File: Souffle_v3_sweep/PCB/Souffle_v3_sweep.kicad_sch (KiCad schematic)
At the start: 86 parts, among them J1 LED, J2 4PIN, J3 OLED, J4 Conn_01x01_Female, J5 Conn_01x01_Female, J6 Conn_01x01, J7 Conn_01x01, SW1 SW_PUSH, SW10 SW_PUSH, SW11 SW_PUSH, SW12 SW_PUSH, SW13 SW_PUSH, SW14 SW_PUSH, SW15 SW_PUSH, SW16 SW_PUSH, SW17 SW_PUSH, SW18 SW_PUSH, SW19 SW_PUSH, SW2 SW_PUSH, SW20 SW_PUSH, SW21 SW_PUSH, SW22 SW_PUSH, SW23 SW_PUSH, SW24 SW_PUSH, SW25 SW_PUSH, SW25b1 RotaryEncoder_Switch, SW26 SW_PUSH, SW27 SW_PUSH, SW28 SW_PUSH, SW29 SW_PUSH, SW3 SW_PUSH, SW30 SW_PUSH, SW31 SW_SPDT, SW4 SW_PUSH, SW5 SW_PUSH, SW6 SW_PUSH, SW7 SW_PUSH, SW8 SW_PUSH, SW9 SW_PUSH, U1 ProMicro

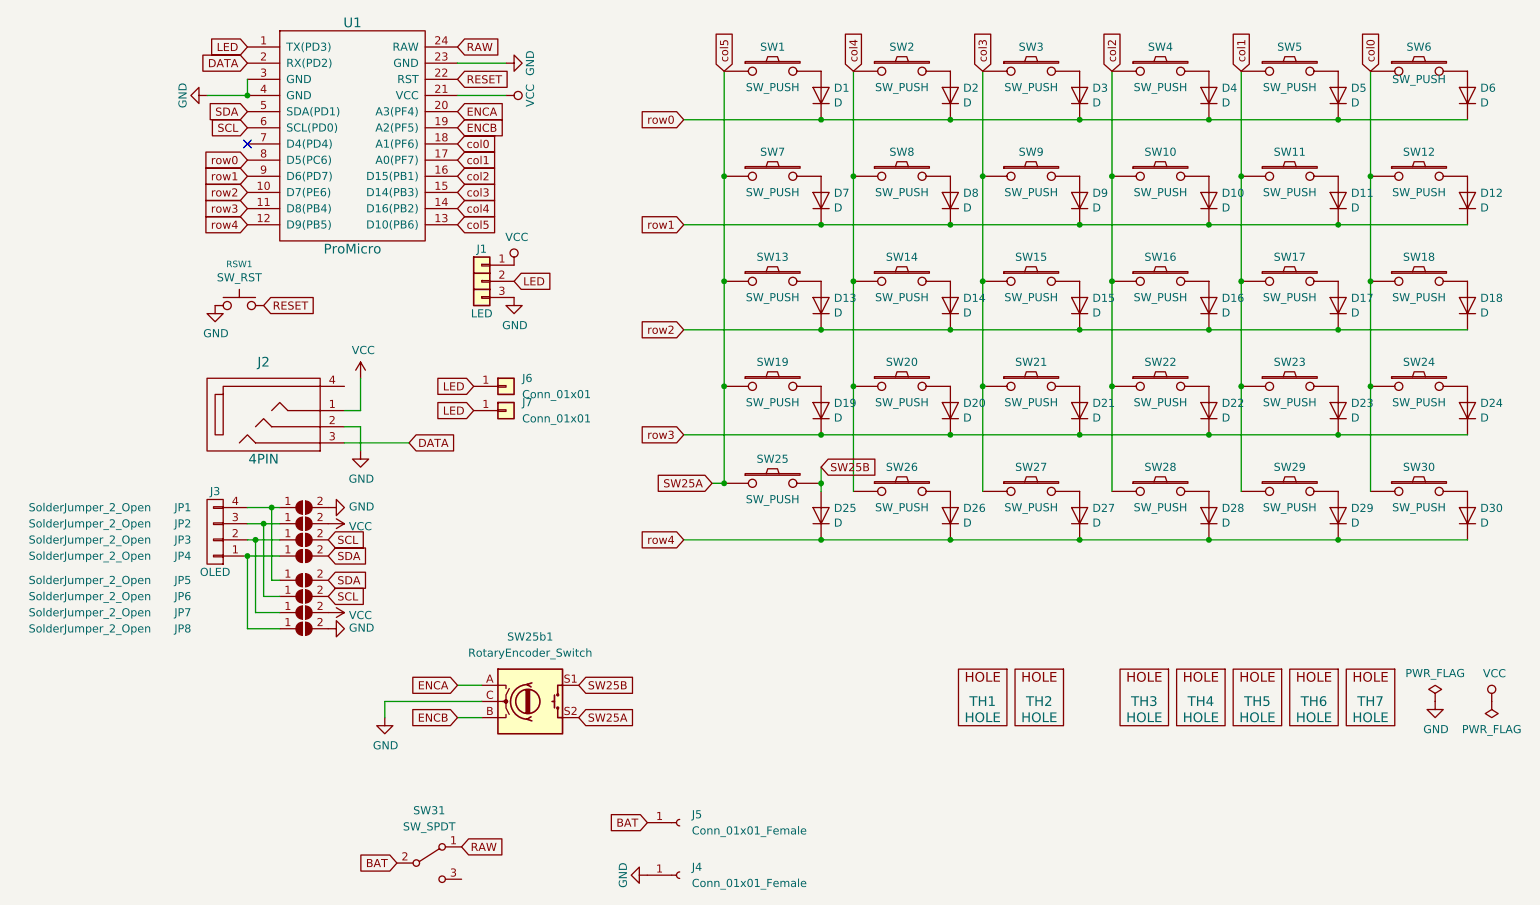
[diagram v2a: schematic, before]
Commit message: V3.2 of the Soufflé keyboard, with reworked NiceView pins
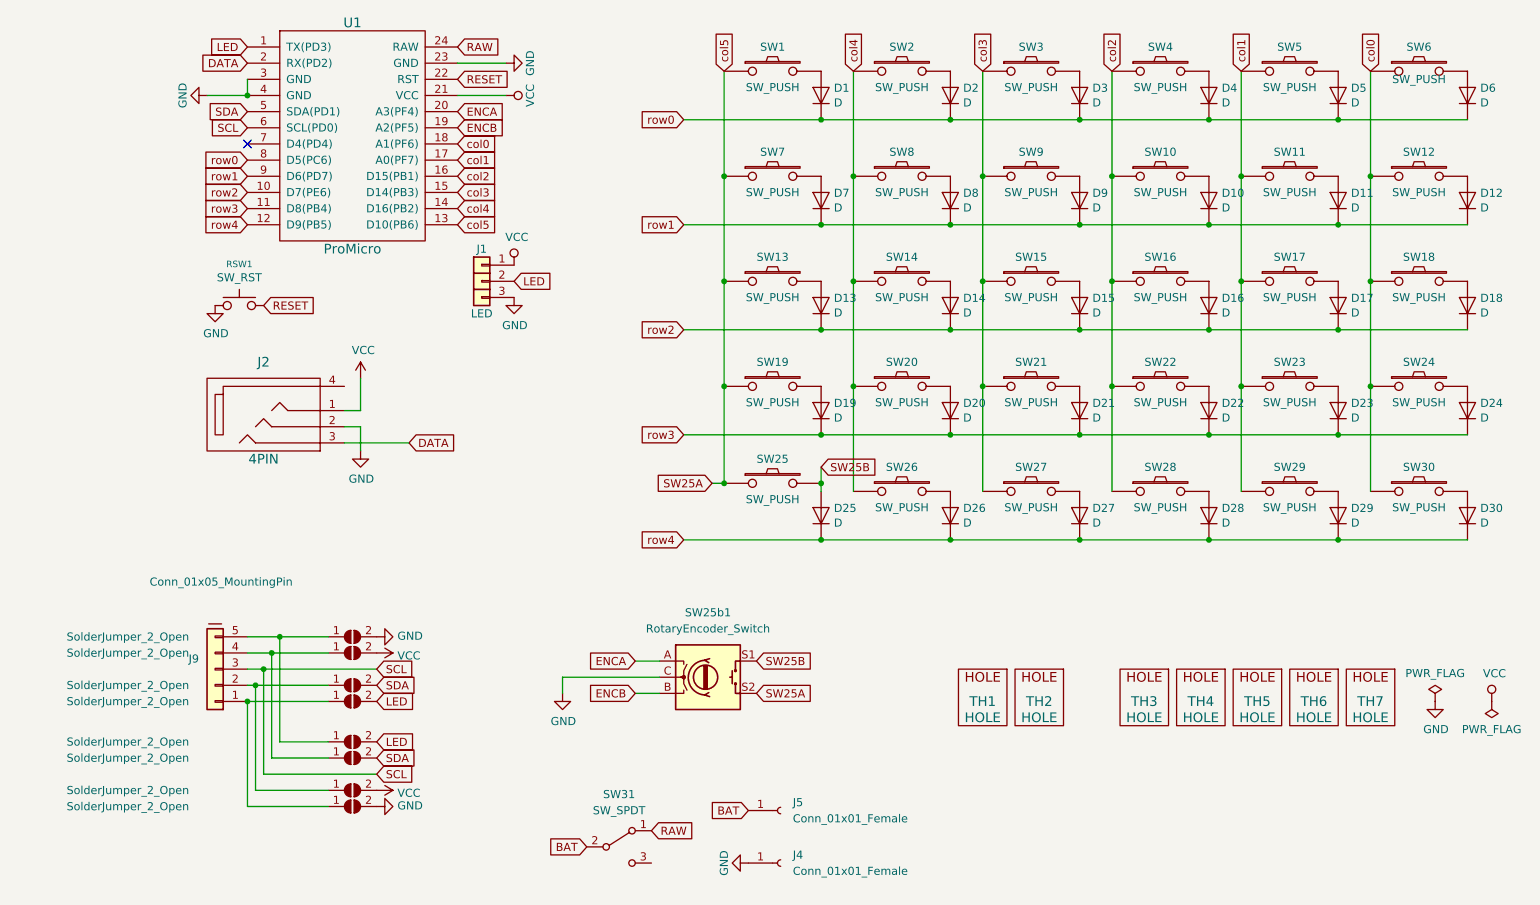
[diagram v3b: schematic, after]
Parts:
- removed J3: OLED, SofleKeyboard-footprint:OLED_4Pin, symbol SofleKeyboard-rescue:OLED-Lily58-cache-Lily58_Pro-rescue
- removed J6, J7: Conn_01x01, Connector_PinSocket_2.00mm:PinSocket_1x01_P2.00mm_Vertical, symbol Connector_Generic:Conn_01x01
- removed JP1, JP2, JP4, JP5, JP6, JP7, JP8: SolderJumper_2_Open, Jumper:SolderJumper-2_P1.3mm_Open_Pad1.0x1.5mm, symbol Jumper:SolderJumper_2_Open
- removed JP3: SolderJumper_2_Open, , symbol Jumper:SolderJumper_2_Open
- added J9: Conn_01x05_MountingPin, Connector_PinHeader_2.54mm:PinHeader_1x05_P2.54mm_Vertical, symbol Connector_Generic_MountingPin:Conn_01x05_MountingPin
- added JP10, JP12, JP13, JP14, JP15, JP17, JP18, JP9: SolderJumper_2_Open, Jumper:SolderJumper-2_P1.3mm_Open_Pad1.0x1.5mm, symbol Jumper:SolderJumper_2_Open
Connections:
- net GND: now also JP18.2 (B), JP9.2 (B)
- net LED: now also JP13.2 (B), JP14.2 (B)
- net SCL: now also J9.3 (Pin_3)
- net SDA: now also JP12.2 (B), JP15.2 (B)
- net VCC: now also JP10.2 (B), JP17.2 (B)
- new net: J9.5 (Pin_5), JP14.1 (A), JP9.1 (A)
- new net: J9.1 (Pin_1), JP13.1 (A), JP18.1 (A)
- new net: J9.2 (Pin_2), JP12.1 (A), JP17.1 (A)
- new net: J9.4 (Pin_4), JP10.1 (A), JP15.1 (A)
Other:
- moved on the sheet: J4, J5, SW25b1, SW31

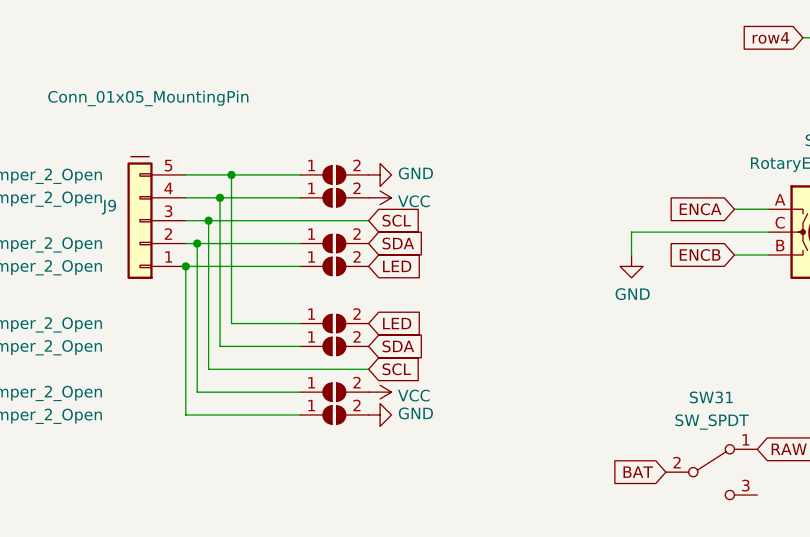
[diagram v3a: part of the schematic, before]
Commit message: Updated and fixed v3.2 as the order of the pads was incorrect. Release v3.2.1 with the fix.
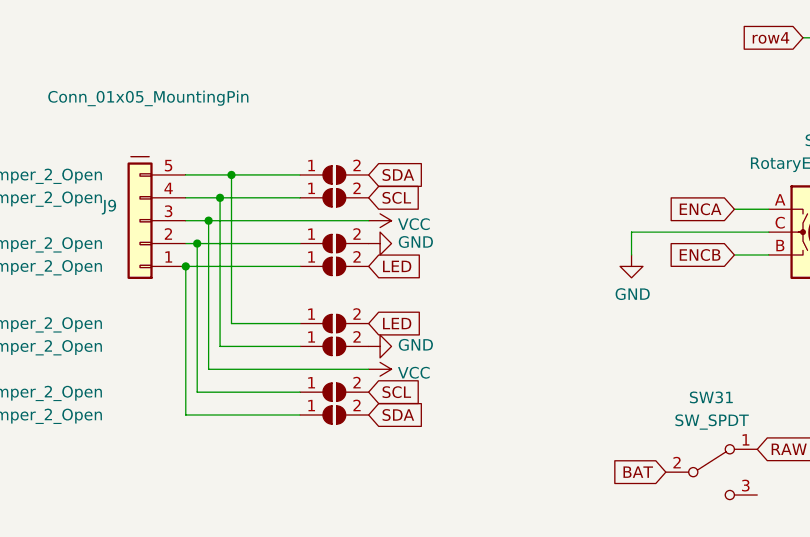
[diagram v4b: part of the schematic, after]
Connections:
- net GND: now also JP12.2 (B), JP15.2 (B); no longer JP18.2 (B), JP9.2 (B)
- net SCL: now also JP10.2 (B), JP17.2 (B); no longer J9.3 (Pin_3)
- net SDA: now also JP18.2 (B), JP9.2 (B); no longer JP12.2 (B), JP15.2 (B)
- net VCC: now also J9.3 (Pin_3); no longer JP10.2 (B), JP17.2 (B)
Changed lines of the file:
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@@
 	(wire
 		(pts
-			(xy 59.69 129.54) (xy 63.5 129.54)
+			(xy 62.23 148.59) (xy 80.01 148.59)
 		)
 		(stroke
@@
 	(wire
 		(pts
-			(xy 72.39 143.51) (xy 64.77 143.51)
+			(xy 59.69 129.54) (xy 63.5 129.54)
 		)
 		(stroke
@@
 	(wire
 		(pts
-			(xy 132.715 102.87) (xy 134.62 102.87)
+			(xy 72.39 143.51) (xy 64.77 143.51)
 		)
 		(stroke
@@
 	(wire
 		(pts
-			(xy 175.26 71.12) (xy 175.26 87.63)
+			(xy 132.715 102.87) (xy 134.62 102.87)
 		)
 		(stroke
@@
 	(wire
 		(pts
-			(xy 62.23 148.59) (xy 80.01 148.59)
+			(xy 175.26 71.12) (xy 175.26 87.63)
 		)
 		(stroke
@@
 	(global_label "SCL"
 		(shape input)
-		(at 80.01 148.59 0)
+		(at 80.01 151.13 0)
 		(fields_autoplaced yes)
 		(effects
@@
 		)
 		(property "Intersheetrefs" "${INTERSHEET_REFS}"
-			(at 5.08 17.78 0)
+			(at 5.08 20.32 0)
 			(effects
 				(font
@@
 	(global_label "SCL"
 		(shape input)
-		(at 80.01 132.08 0)
+		(at 80.01 129.54 0)
 		(fields_autoplaced yes)
 		(effects
@@
 		)
 		(property "Intersheetrefs" "${INTERSHEET_REFS}"
-			(at 5.08 1.27 0)
+			(at 5.08 -1.27 0)
 			(effects
 				(font
@@
 	(global_label "SDA"
 		(shape input)
-		(at 80.01 134.62 0)
+		(at 80.01 127 0)
 		(fields_autoplaced yes)
 		(effects
@@
 		)
 		(property "Intersheetrefs" "${INTERSHEET_REFS}"
-			(at 5.08 1.27 0)
+			(at 5.08 -6.35 0)
 			(effects
 				(font
@@
 	(global_label "SDA"
 		(shape input)
-		(at 80.01 146.05 0)
+		(at 80.01 153.67 0)
 		(fields_autoplaced yes)
 		(effects
@@
 		)
 		(property "Intersheetrefs" "${INTERSHEET_REFS}"
-			(at 5.08 12.7 0)
+			(at 5.08 20.32 0)
 			(effects
 				(font
@@
 	(symbol
 		(lib_id "power:VCC")
-		(at 80.01 151.13 270)
+		(at 80.01 148.59 270)
 		(unit 1)
 		(exclude_from_sim no)
@@
 		(dnp no)
 		(property "Reference" "#PWR04"
-			(at 76.2 151.13 0)
+			(at 76.2 148.59 0)
 			(effects
 				(font
@@
 		)
 		(property "Value" "VCC"
-			(at 83.2612 151.5618 90)
+			(at 83.2612 149.0218 90)
 			(effects
 				(font
@@
 		)
 		(property "Footprint" ""
-			(at 80.01 151.13 0)
+			(at 80.01 148.59 0)
 			(effects
 				(font
@@
 		)
 		(property "Datasheet" ""
-			(at 80.01 151.13 0)
+			(at 80.01 148.59 0)
 			(effects
 				(font
@@
 		)
 		(property "Description" ""
-			(at 80.01 151.13 0)
+			(at 80.01 148.59 0)
 			(effects
 				(font
@@
 	(symbol
 		(lib_id "power:VCC")
-		(at 80.01 129.54 270)
+		(at 80.01 132.08 270)
 		(unit 1)
 		(exclude_from_sim no)
@@
 		(dnp no)
 		(property "Reference" "#PWR03"
-			(at 76.2 129.54 0)
+			(at 76.2 132.08 0)
 			(effects
 				(font
@@
 		)
 		(property "Value" "VCC"
-			(at 83.2612 129.9718 90)
+			(at 83.2612 132.5118 90)
 			(effects
 				(font
@@
 		)
 		(property "Footprint" ""
-			(at 80.01 129.54 0)
+			(at 80.01 132.08 0)
 			(effects
 				(font
@@
 		)
 		(property "Datasheet" ""
-			(at 80.01 129.54 0)
+			(at 80.01 132.08 0)
 			(effects
 				(font
@@
 		)
 		(property "Description" ""
-			(at 80.01 129.54 0)
+			(at 80.01 132.08 0)
 			(effects
 				(font
@@
 	(symbol
 		(lib_id "power:GND")
-		(at 80.01 127 90)
+		(at 80.01 134.62 90)
 		(unit 1)
 		(exclude_from_sim no)
@@
 		(dnp no)
 		(property "Reference" "#PWR01"
-			(at 86.36 127 0)
+			(at 86.36 134.62 0)
 			(effects
 				(font
@@
 		)
 		(property "Value" "GND"
-			(at 83.2612 126.873 90)
+			(at 83.2612 134.493 90)
 			(effects
 				(font
@@
 		)
 		(property "Footprint" ""
-			(at 80.01 127 0)
+			(at 80.01 134.62 0)
 			(effects
 				(font
@@
 		)
 		(property "Datasheet" ""
-			(at 80.01 127 0)
+			(at 80.01 134.62 0)
 			(effects
 				(font
@@
 		)
 		(property "Description" ""
-			(at 80.01 127 0)
+			(at 80.01 134.62 0)
 			(effects
 				(font
@@
 	(symbol
 		(lib_id "power:GND")
-		(at 80.01 153.67 90)
+		(at 80.01 146.05 90)
 		(unit 1)
 		(exclude_from_sim no)
@@
 		(dnp no)
 		(property "Reference" "#PWR02"
-			(at 86.36 153.67 0)
+			(at 86.36 146.05 0)
 			(effects
 				(font
@@
 		)
 		(property "Value" "GND"
-			(at 83.2612 153.543 90)
+			(at 83.2612 145.923 90)
 			(effects
 				(font
@@
 		)
 		(property "Footprint" ""
-			(at 80.01 153.67 0)
+			(at 80.01 146.05 0)
 			(effects
 				(font
@@
 		)
 		(property "Datasheet" ""
-			(at 80.01 153.67 0)
+			(at 80.01 146.05 0)
 			(effects
 				(font
@@
 		)
 		(property "Description" ""
-			(at 80.01 153.67 0)
+			(at 80.01 146.05 0)
 			(effects
 				(font
